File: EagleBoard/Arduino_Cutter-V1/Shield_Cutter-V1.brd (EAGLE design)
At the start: 100 x 80 mm, 83 parts, among them IC1 L298P, IC2 REG1117, K1 AQY21SOP, K2 AQY21SOP, U1 ARDUINOR3-DIMENSION, X1 2514-, X2 22-23-2041, X3 22-23-2021, X4 22-23-2021

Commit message: Feat: pcb routed
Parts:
- removed S1: (no value), switch-omron:B3F-10XX
- added RESET: (no value), switch-omron:B3F-10XX
- moved R12 209.1 mm to (61.0, 20.3), flipped to the bottom, turned to 180 degrees
- moved R5 208.2 mm to (62.2, 14.0), flipped to the bottom, turned to 180 degrees
- moved LED5 207.1 mm to (55.2, 9.40)
- moved R9 203.2 mm to (57.1, 6.35), turned to 90 degrees
- moved R4 202.2 mm to (62.2, 6.35), turned to 90 degrees
- moved R10 195.2 mm to (59.7, 6.35), turned to 90 degrees
- moved R6 192.2 mm to (62.2, 6.35), flipped to the bottom, turned to 90 degrees
- moved R7 188.1 mm to (62.2, 11.4), flipped to the bottom, turned to 180 degrees
- moved R26 183.5 mm to (45.1, 16.1), flipped to the bottom, turned to 90 degrees
- moved R27 182.2 mm to (45.1, 24.5), flipped to the bottom, turned to 270 degrees
- moved R3 179.1 mm to (61.0, 17.8), flipped to the bottom, turned to 180 degrees
- moved R25 177.1 mm to (51.2, 27.6), flipped to the bottom
- moved X4 176.9 mm to (66.0, 12.7), turned to 270 degrees
- moved JP1 171.8 mm to (53.3, 15.2), turned to 270 degrees
- moved R30 171.5 mm to (2.54, 15.2)
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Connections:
- removed net N$25: SV9.1
- net BUTTON_INT: now also U1.D2; no longer U1.D3
- net DOWN_BUT: now also D12.2, R26.2, U1.A1; no longer D11.3, R25.2, U1.A2
- net E-STOP: now also SV9.1
- net GND: now also RESET.3, RESET.4; no longer S1.3, S1.4
- net LCD_D4: now also X1.8; no longer X1.7
- net LCD_D5: now also X1.7; no longer X1.8
- net LCD_D6: now also X1.10; no longer X1.9
- net LCD_D7: now also X1.9; no longer X1.10
- net RESET: now also RESET.1, RESET.2; no longer S1.1, S1.2
- net RUN_BUT: now also D12.3, R27.2, U1.A2; no longer D12.2, R26.2, U1.A3
- net SELECT_BUT: now also D11.3, R25.2, U1.A3; no longer D12.3, R27.2, U1.A4
- net SOL_CUT: now also U1.A4; no longer U1.A0
- net SOL_PIERCE: now also U1.A5; no longer U1.A1
- net SPEED_POT: now also U1.A0; no longer U1.A5
- net STEPER1: now also U1.D10; no longer U1.D13
- net STEPER2: now also U1.D11; no longer U1.D12
- net STEPER3: now also U1.D12; no longer U1.D11
- net STEPER4: now also U1.D13; no longer U1.D10
- net UP_BUT: now also U1.D3; no longer U1.D2
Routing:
- net +5V: track 0.00 -> 200.8 mm, vias 0 -> 9
- net VMOT: track 0.00 -> 100.3 mm, vias 0 -> 4
- net GND: track 15.5 -> 64.5 mm, vias 0 -> 9
- net STEPER1: track 0.00 -> 46.7 mm, vias 0 -> 2
- net BUTTON_INT: track 0.00 -> 45.5 mm, vias 0 -> 2
- net ENABLEA: track 0.00 -> 44.2 mm, vias 0 -> 2
- net SELECT_BUT: track 0.00 -> 39.9 mm, vias 0 -> 2
- net OUT3: track 0.00 -> 37.6 mm, vias 0 -> 1
- net STEPER2: track 0.00 -> 36.6 mm
- net OUT2: track 0.00 -> 34.9 mm, vias 0 -> 1
- net OUT4: track 0.00 -> 31.7 mm, vias 0 -> 1
- net OUT1: track 0.00 -> 31.1 mm, vias 0 -> 1
- net ENCODER1: track 0.00 -> 30.2 mm
- net N$10: track 0.00 -> 28.2 mm
- net RUN_BUT: track 0.00 -> 26.9 mm, vias 0 -> 1
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
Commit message: Feat: pcb routed
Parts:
- removed U$1: DISCLAIMER, SmartPrj:DISCLAIMER
- D11, D12: value (none) -> 40v
- R24: value (none) -> 10k
- moved FID2 1.80 mm to (15.2, 21.6)
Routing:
- net +5V: track 200.8 -> 207.9 mm, vias 9 -> 10
- net VMOT: track 100.3 -> 96.5 mm
- net GND: track 64.5 -> 66.0 mm
- net RESET: track 16.2 -> 15.9 mm, vias 1 -> 0
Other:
- board size 100 x 80 mm -> 68.9 x 53.7 mm

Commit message: Feat: pcb routed
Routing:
- net GND: track 66.0 -> 77.1 mm, vias 9 -> 10
- net N$19: track 4.49 -> 11.3 mm
- net +5V: track 207.9 -> 213.4 mm
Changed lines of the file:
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@@
 <setting verticaltext="up"/>
 </settings>
-<grid distance="50" unitdist="mil" unit="mil" style="lines" multiple="1" display="yes" altdistance="5" altunitdist="mil" altunit="mil"/>
+<grid distance="25" unitdist="mil" unit="mil" style="lines" multiple="1" display="yes" altdistance="5" altunitdist="mil" altunit="mil"/>
 <layers>
 <layer number="1" name="Top" color="4" fill="1" visible="yes" active="yes"/>
@@
 <wire x1="19.05" y1="41.91" x2="19.05" y2="41.31" width="0.6096" layer="16"/>
 <wire x1="19.05" y1="41.31" x2="19.72" y2="40.64" width="0.6096" layer="16"/>
+<wire x1="13.97" y1="30.06" x2="13.55" y2="30.06" width="0.508" layer="1"/>
+<wire x1="12.7" y1="29.21" x2="13.55" y2="30.06" width="0.508" layer="1"/>
+<wire x1="11.85" y1="24.55" x2="11.43" y2="24.55" width="0.508" layer="1"/>
+<wire x1="11.85" y1="24.55" x2="12.7" y2="25.4" width="0.508" layer="1"/>
+<wire x1="12.7" y1="25.4" x2="12.7" y2="29.21" width="0.508" layer="1"/>
+<wire x1="11.43" y1="24.55" x2="10.58" y2="24.55" width="0.508" layer="1"/>
+<wire x1="10.58" y1="24.55" x2="10.16" y2="24.13" width="0.508" layer="1"/>
+<wire x1="10.16" y1="24.13" x2="10.16" y2="21.569" width="0.508" layer="1"/>
+<via x="10.16" y="21.569" extent="1-16" drill="0.55"/>
 <wire x1="60.96" y1="34.33" x2="63.5" y2="47.41" width="0" layer="19" extent="16-16"/>
 <wire x1="65.239" y1="29.337" x2="60.96" y2="34.33" width="0" layer="19" extent="16-16"/>
@@
 <wire x1="19.05" y1="36.6268" x2="13.97" y2="35.98" width="0" layer="19" extent="1-1"/>
 <wire x1="19.72" y1="36.83" x2="19.05" y2="36.6268" width="0" layer="19" extent="1-16"/>
+<wire x1="12.4206" y1="16.2306" x2="10.16" y2="21.569" width="0" layer="19" extent="1-1"/>
 <wire x1="11.43" y1="41.49" x2="13.97" y2="35.98" width="0" layer="19" extent="1-1"/>
-<wire x1="11.43" y1="24.55" x2="13.97" y2="30.06" width="0" layer="19" extent="1-1"/>
-<wire x1="13.3604" y1="16.2306" x2="17.78" y2="20.549" width="0" layer="19" extent="1-1"/>
 <wire x1="33.02" y1="22.86" x2="31.8262" y2="29.21" width="0" layer="19" extent="1-1"/>
 <wire x1="3.14" y1="13.97" x2="11.43" y2="15.24" width="0" layer="19" extent="1-16"/>
@@
 <wire x1="26.67" y1="5.08" x2="32.89" y2="5.08" width="1.016" layer="1"/>
 <wire x1="32.89" y1="5.08" x2="33.02" y2="4.95" width="1.016" layer="1"/>
-<wire x1="33.02" y1="4.95" x2="37.97" y2="4.95" width="1.016" layer="1"/>
+<wire x1="36.898775" y1="4.95" x2="33.02" y2="4.95" width="1.016" layer="1"/>
+<wire x1="36.898775" y1="4.95" x2="37.97" y2="4.95" width="1.016" layer="1"/>
 <wire x1="37.97" y1="4.95" x2="39.37" y2="6.35" width="1.016" layer="1"/>
 <wire x1="30.48" y1="12.7" x2="30.06" y2="12.28" width="0.6096" layer="16"/>
@@
 <wire x1="47.12419375" y1="39.50419375" x2="46.85580625" y2="39.50419375" width="0.6096" layer="16"/>
 <wire x1="48.0778" y1="38.5505875" x2="47.12419375" y2="39.50419375" width="0.6096" layer="16"/>
-<wire x1="37.97" y1="4.95" x2="36.83" y2="5.5" width="0" layer="19" extent="1-1"/>
-<wire x1="20.19" y1="10.16" x2="20.19" y2="9.00269375" width="0" layer="19" extent="1-1"/>
-<wire x1="19.05" y1="10.16" x2="20.19" y2="10.16" width="0" layer="19" extent="1-1"/>
-<wire x1="29.21" y1="4.95" x2="26.67" y2="5.08" width="0" layer="19" extent="1-1"/>
+<wire x1="26.67" y1="5.08" x2="26.8" y2="4.95" width="0.6096" layer="1"/>
+<wire x1="26.8" y1="4.95" x2="29.21" y2="4.95" width="0.6096" layer="1"/>
+<wire x1="36.83" y1="5.5" x2="36.898775" y2="5.431225" width="0.6096" layer="1"/>
+<wire x1="36.898775" y1="5.431225" x2="36.898775" y2="4.95" width="0.6096" layer="1"/>
+<wire x1="20.19" y1="10.16" x2="20.19" y2="9.00269375" width="0.6096" layer="1"/>
+<wire x1="19.05" y1="10.16" x2="20.19" y2="10.16" width="1.016" layer="1"/>
 </signal>
 <signal name="VIN" class="2">
@@
 <contactref element="U1" pad="RESET"/>
 <wire x1="18.3388" y1="2.8194" x2="24.8412" y2="2.8194" width="0.6096" layer="16"/>
-<wire x1="24.8412" y1="2.8194" x2="25.1206" y2="2.8194" width="0" layer="19" extent="1-16"/>
 <wire x1="25.1206" y1="2.8194" x2="27.1272" y2="0.8128" width="0.6096" layer="16"/>
 <wire x1="27.1272" y1="0.8128" x2="31.2928" y2="0.8128" width="0.6096" layer="16"/>
 <wire x1="31.2928" y1="0.8128" x2="33.02" y2="2.54" width="0.6096" layer="16"/>
-<wire x1="25.1206" y1="2.8194" x2="25.1206" y2="2.8194" width="0" layer="19" extent="1-16"/>
+<wire x1="24.8412" y1="2.8194" x2="25.1206" y2="2.8194" width="0.6096" layer="16"/>
 </signal>
 <signal name="N$1">
@@
 <contactref element="K1" pad="3"/>
 <contactref element="R3" pad="1"/>
-<wire x1="60.11" y1="20.32" x2="60.11" y2="17.78" width="0.8128" layer="16"/>
+<wire x1="60.11" y1="19.036215625" x2="60.11" y2="20.32" width="0.8128" layer="16"/>
 <via x="60.071" y="19.05" extent="1-16" drill="0.55"/>
 <wire x1="60.071" y1="19.05" x2="60.071" y2="17.351" width="0.8128" layer="1"/>
 <wire x1="60.071" y1="17.351" x2="59.69" y2="16.97" width="0.8128" layer="1"/>
-<wire x1="60.071" y1="17.351" x2="60.11" y2="17.78" width="0" layer="19" extent="1-16"/>
+<wire x1="60.11" y1="17.78" x2="60.11" y2="19.036215625" width="0.6096" layer="16"/>
+<wire x1="60.071" y1="19.05" x2="60.11" y2="19.036215625" width="0" layer="19" extent="16-16"/>
 </signal>
 <signal name="UP_BUT">
@@
 <wire x1="45.046" y1="25.4" x2="41.91" y2="25.4" width="0.6096" layer="16"/>
 <wire x1="41.91" y1="25.4" x2="41.91" y2="25.38" width="0.6096" layer="16"/>
-<wire x1="37.299" y1="19.939" x2="37.299" y2="22.059" width="0" layer="19" extent="1-16"/>
-<wire x1="37.299" y1="22.059" x2="40.64" y2="25.4" width="0" layer="19" extent="1-16"/>
 <wire x1="40.64" y1="25.4" x2="41.89" y2="25.4" width="0.6096" layer="1"/>
 <wire x1="41.89" y1="25.4" x2="41.91" y2="25.38" width="0.6096" layer="1"/>
+<wire x1="37.299" y1="19.939" x2="39.37" y2="22.01" width="0.6096" layer="1"/>
+<wire x1="39.37" y1="22.01" x2="39.37" y2="24.13" width="0.6096" layer="1"/>
+<wire x1="39.37" y1="24.13" x2="40.64" y2="25.4" width="0.6096" layer="1"/>
 </signal>
 <signal name="IOREF">

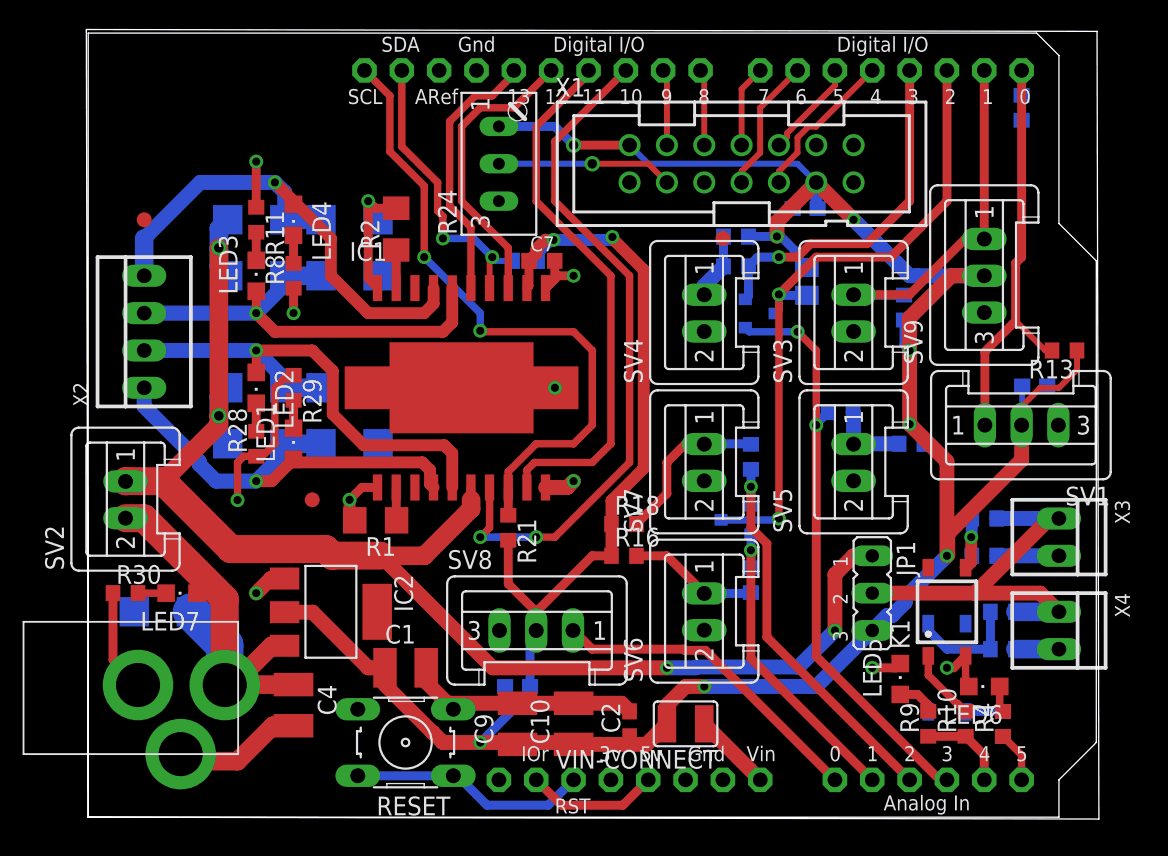
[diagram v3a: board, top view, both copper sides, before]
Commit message: Feat: add pcb ground plane
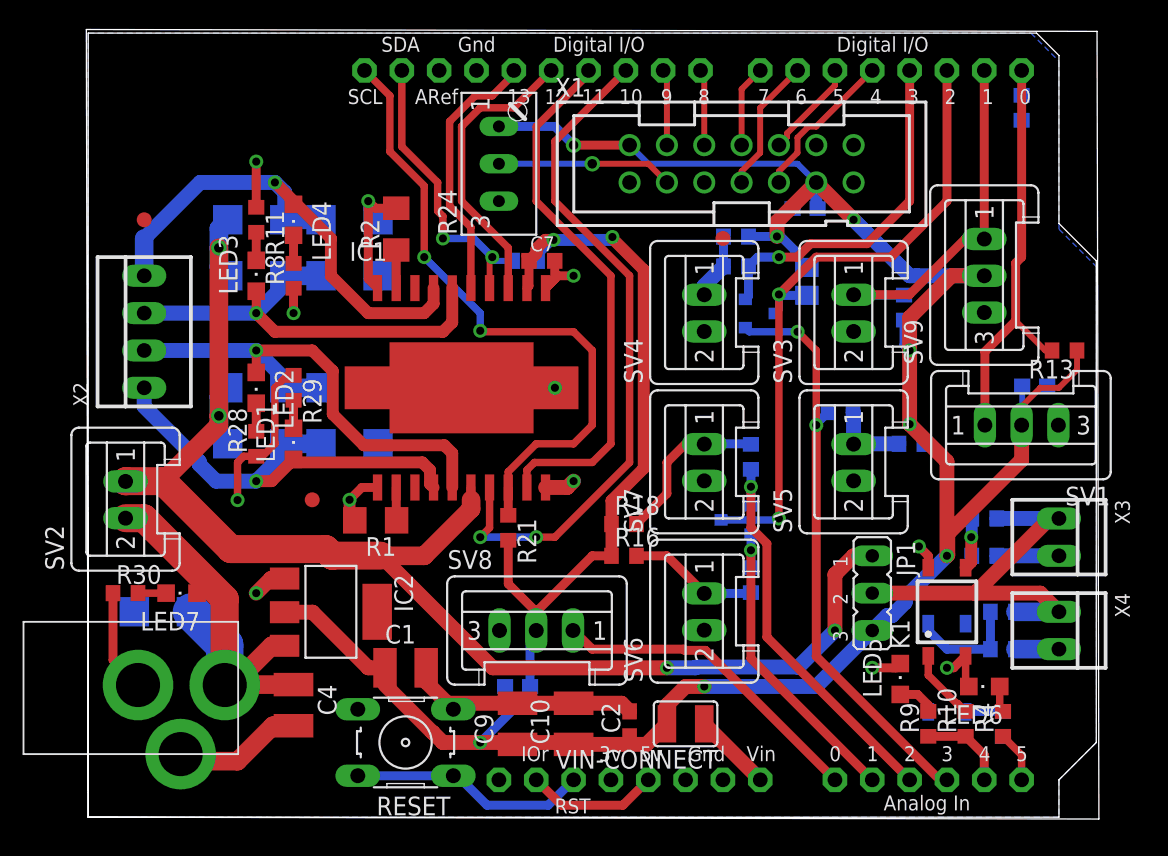
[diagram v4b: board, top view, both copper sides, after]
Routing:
- net GND: track 77.1 -> 95.8 mm, vias 10 -> 11
- added copper zone on layer 16, net GND
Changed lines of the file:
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@@
 <wire x1="10.16" y1="24.13" x2="10.16" y2="21.569" width="0.508" layer="1"/>
 <via x="10.16" y="21.569" extent="1-16" drill="0.55"/>
-<wire x1="60.96" y1="34.33" x2="63.5" y2="47.41" width="0" layer="19" extent="16-16"/>
-<wire x1="65.239" y1="29.337" x2="60.96" y2="34.33" width="0" layer="19" extent="16-16"/>
-<wire x1="66" y1="26.67" x2="65.239" y2="29.337" width="0" layer="19" extent="16-16"/>
-<wire x1="52.07" y1="33.04" x2="60.96" y2="34.33" width="0" layer="19" extent="1-1"/>
-<wire x1="47.918" y1="41.402" x2="52.07" y2="33.04" width="0" layer="19" extent="16-16"/>
-<wire x1="49.53" y1="45.72" x2="47.918" y2="41.402" width="0" layer="19" extent="16-16"/>
-<wire x1="41.91" y1="43.18" x2="47.918" y2="41.402" width="0" layer="19" extent="16-16"/>
-<wire x1="36.83" y1="43.18" x2="41.91" y2="43.18" width="0" layer="19" extent="1-1"/>
-<wire x1="31.736" y1="37.846" x2="36.83" y2="43.18" width="0" layer="19" extent="1-1"/>
-<wire x1="27.94" y1="41.91" x2="31.736" y2="37.846" width="0" layer="19" extent="1-1"/>
-<wire x1="31.8262" y1="29.21" x2="31.115" y2="35.9918" width="0" layer="19" extent="1-1"/>
-<wire x1="25.4" y1="29.21" x2="31.8262" y2="29.21" width="0" layer="19" extent="1-1"/>
-<wire x1="19.72" y1="29.21" x2="25.4" y2="29.21" width="0" layer="19" extent="1-16"/>
-<wire x1="18.9738" y1="29.21" x2="19.72" y2="29.21" width="0" layer="19" extent="1-16"/>
-<wire x1="19.72" y1="25.4" x2="19.72" y2="29.21" width="0" layer="19" extent="16-16"/>
-<wire x1="19.685" y1="22.4282" x2="19.72" y2="25.4" width="0" layer="19" extent="1-16"/>
-<wire x1="13.97" y1="30.06" x2="18.9738" y2="29.21" width="0" layer="19" extent="1-1"/>
-<wire x1="13.97" y1="34.29" x2="13.97" y2="30.06" width="0" layer="19" extent="1-1"/>
-<wire x1="19.05" y1="36.6268" x2="13.97" y2="35.98" width="0" layer="19" extent="1-1"/>
-<wire x1="19.72" y1="36.83" x2="19.05" y2="36.6268" width="0" layer="19" extent="1-16"/>
-<wire x1="12.4206" y1="16.2306" x2="10.16" y2="21.569" width="0" layer="19" extent="1-1"/>
-<wire x1="11.43" y1="41.49" x2="13.97" y2="35.98" width="0" layer="19" extent="1-1"/>
-<wire x1="33.02" y1="22.86" x2="31.8262" y2="29.21" width="0" layer="19" extent="1-1"/>
-<wire x1="3.14" y1="13.97" x2="11.43" y2="15.24" width="0" layer="19" extent="1-16"/>
-<wire x1="1.69" y1="15.24" x2="3.14" y2="13.97" width="0" layer="19" extent="1-16"/>
-<wire x1="6.29" y1="4.29" x2="3.39" y2="8.99" width="0" layer="19" extent="1-1"/>
-<wire x1="18.3388" y1="7.3406" x2="13.97" y2="6.22" width="0" layer="19" extent="1-1"/>
-<wire x1="22.99" y1="9.1918" x2="18.3388" y2="7.3406" width="0" layer="19" extent="1-1"/>
-<wire x1="29.21" y1="7.75" x2="33.02" y2="7.75" width="0" layer="19" extent="1-1"/>
-<wire x1="28.36" y1="8.89" x2="29.21" y2="7.75" width="0" layer="19" extent="1-16"/>
-<wire x1="28.36" y1="12.32" x2="28.36" y2="8.89" width="0" layer="19" extent="16-16"/>
-<wire x1="40.64" y1="2.54" x2="36.83" y2="7.2" width="0" layer="19" extent="1-1"/>
-<wire x1="43.18" y1="2.54" x2="40.64" y2="2.54" width="0" layer="19" extent="1-1"/>
-<wire x1="41.91" y1="12.72" x2="36.83" y2="7.2" width="0" layer="19" extent="1-1"/>
-<wire x1="41.91" y1="22.88" x2="33.02" y2="22.86" width="0" layer="19" extent="1-1"/>
-<wire x1="26.416" y1="50.8" x2="27.94" y2="41.91" width="0" layer="19" extent="1-1"/>
-<wire x1="41.91" y1="33.04" x2="33.02" y2="36.83" width="0" layer="19" extent="1-1"/>
-<wire x1="52.07" y1="22.88" x2="52.07" y2="33.04" width="0" layer="19" extent="1-1"/>
-<wire x1="57.15" y1="16.97" x2="52.07" y2="22.88" width="0" layer="19" extent="1-1"/>
-<wire x1="59.69" y1="13.16" x2="57.15" y2="16.97" width="0" layer="19" extent="1-16"/>
-<wire x1="59.69" y1="10.97" x2="59.69" y2="13.16" width="0" layer="19" extent="1-16"/>
-<wire x1="57.15" y1="7.16" x2="59.69" y2="8.89" width="0" layer="19" extent="1-16"/>
-<wire x1="55.245" y1="10.448" x2="58.42" y2="10.16" width="0" layer="19" extent="1-1"/>
+<polygon width="0.6096" layer="16" isolate="0.4064">
+<vertex x="0" y="53.34"/>
+<vertex x="64.135" y="53.34"/>
+<vertex x="66.04" y="51.435"/>
+<vertex x="66.04" y="40.005"/>
+<vertex x="68.58" y="37.465"/>
+<vertex x="68.58" y="5.08"/>
+<vertex x="66.04" y="2.54"/>
+<vertex x="66.04" y="0"/>
+<vertex x="0" y="0"/>
+</polygon>
+<wire x1="57.15" y1="16.97" x2="57.15" y2="17.78" width="0.6096" layer="1"/>
+<wire x1="57.15" y1="17.78" x2="56.515" y2="18.415" width="0.6096" layer="1"/>
+<via x="56.515" y="18.415" extent="1-16" drill="0.55"/>
+<wire x1="30.6622" y1="29.21" x2="18.9738" y2="29.21" width="0.6096" layer="1"/>
+<wire x1="25.4" y1="29.21" x2="30.6622" y2="29.21" width="0.6096" layer="1"/>
+<wire x1="30.6622" y1="29.21" x2="31.8262" y2="29.21" width="0" layer="19" extent="1-1"/>
+<wire x1="19.72" y1="29.21" x2="18.9738" y2="29.21" width="0" layer="19" extent="1-16"/>
+<wire x1="29.21" y1="7.75" x2="28.36" y2="8.89" width="0" layer="19" extent="1-16"/>
+<wire x1="59.69" y1="13.16" x2="59.69" y2="10.97" width="0" layer="19" extent="1-16"/>
 </signal>
 <signal name="+5V" class="1">
@@
 <wire x1="8.89" y1="26.67" x2="8.89" y2="27.305" width="1.27" layer="1"/>
 <wire x1="8.89" y1="27.305" x2="8.89" y2="38.735" width="1.27" layer="1"/>
-<wire x1="8.89" y1="38.735" x2="8.89" y2="39.37" width="0" layer="19" extent="1-16"/>
 <via x="8.89" y="38.735" extent="1-16" drill="0.65"/>
 <via x="8.89" y="27.305" extent="1-16" drill="0.65"/>
@@
 <signal name="N$20">
 </signal>
-<signal name="N$21">
-<wire x1="9.525" y1="38.735" x2="6.985" y2="27.305" width="0" layer="19" extent="1-16"/>
-<wire x1="6.985" y1="27.305" x2="10.16" y2="26.67" width="0" layer="19" extent="1-16"/>
-</signal>
 <signal name="N$22">
